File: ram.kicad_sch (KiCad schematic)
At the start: 1 part, among them U20 74LS157

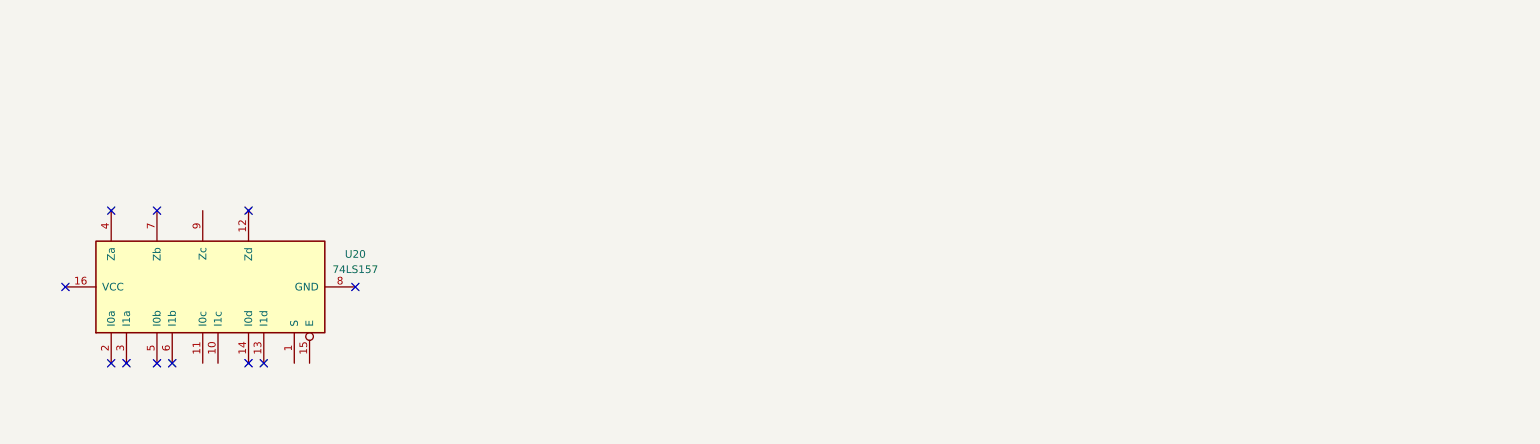
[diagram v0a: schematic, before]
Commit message: Made the ram module as well as set up a custom symbol for the 74f189sj chip.
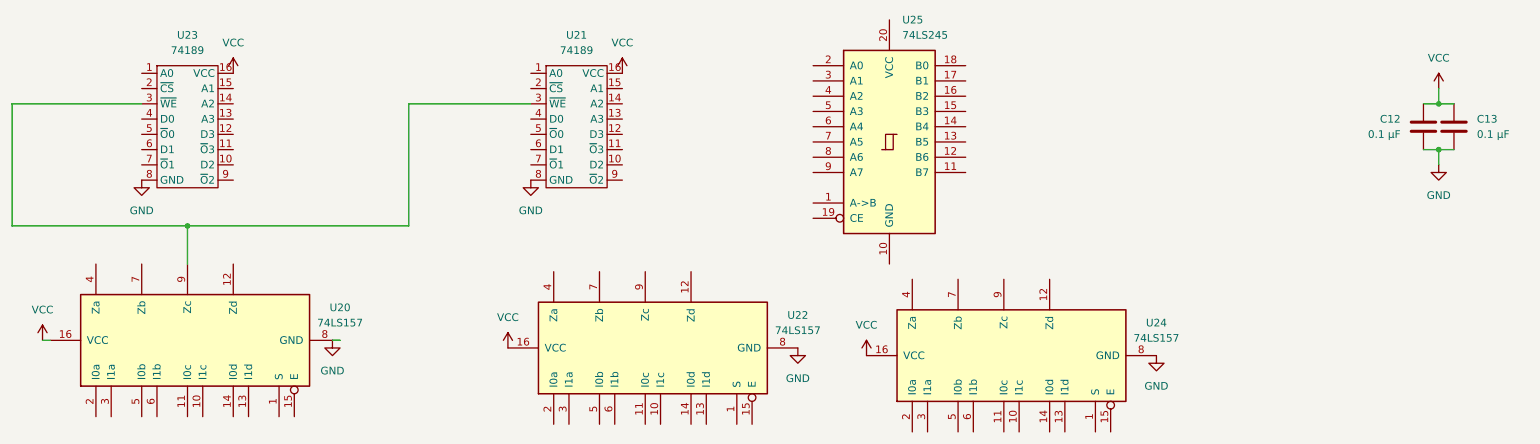
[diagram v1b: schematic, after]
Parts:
- added C12, C13: 0.1 µF, symbol Device:C
- added U21, U23: 74189, symbol Custom:74F189SJ
- added U22, U24: 74LS157, symbol 74xx:74LS157
- added U25: 74LS245, symbol 74xx:74LS245
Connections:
- net VCC: now reaches U20.16 (VCC)
- net VCC: now also C12.1, C13.1, U21.16 (VCC), U22.16 (VCC), U23.16 (VCC), U24.16 (VCC)
- net GND: now reaches U20.8 (GND)
- net GND: now also C12.2, C13.2, U21.8 (GND), U22.8 (GND), U23.8 (GND), U24.8 (GND)
- net at U20.9 (Zc): now also U21.3 (~{WE}), U23.3 (~{WE})
- no-connect marks 11 -> 0

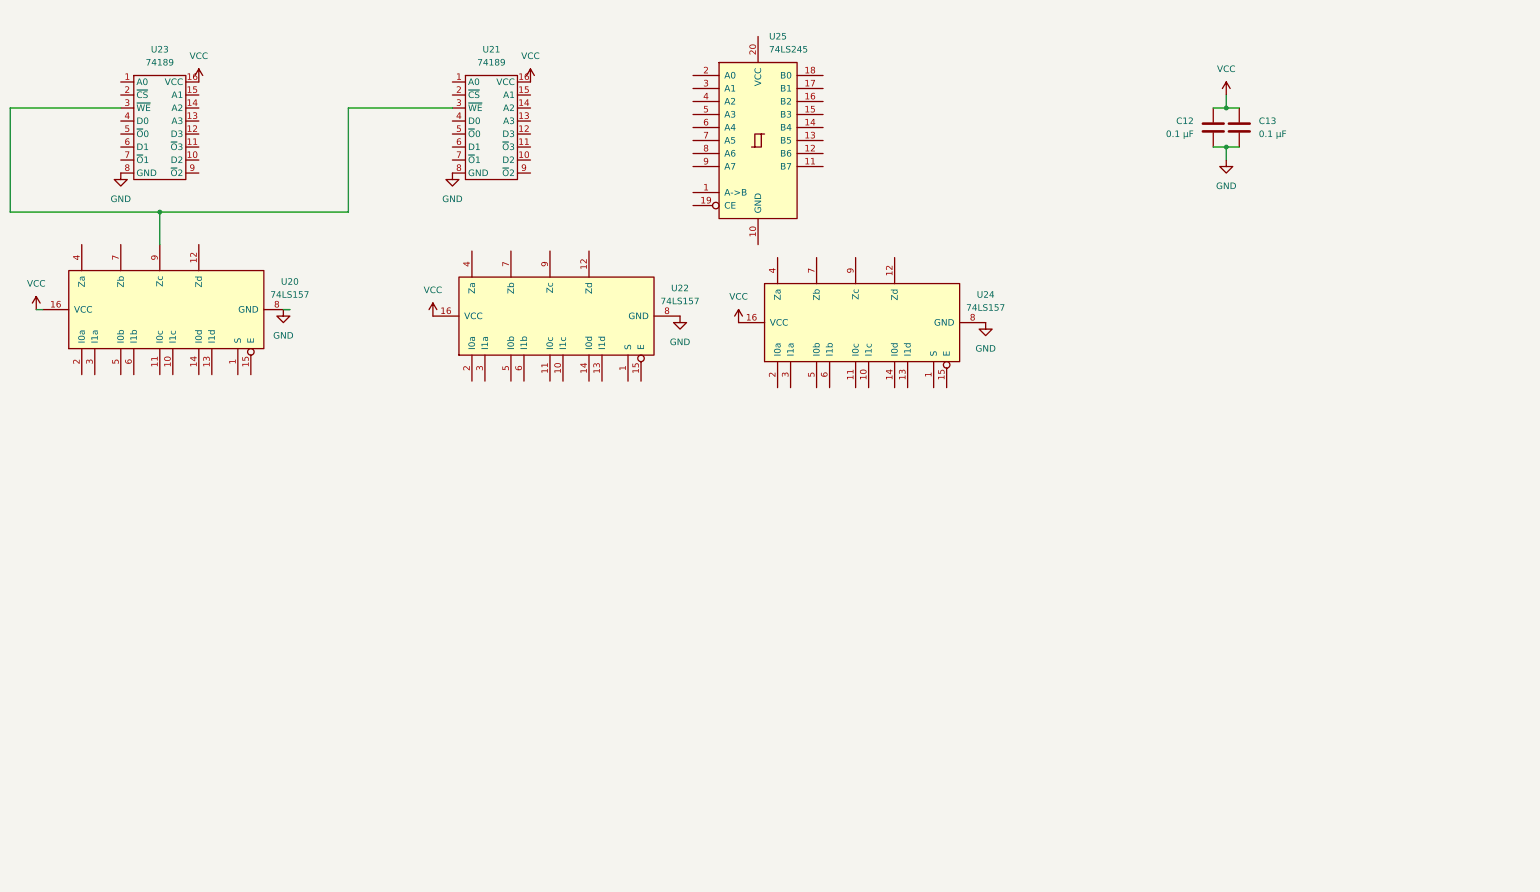
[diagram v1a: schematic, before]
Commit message: Added the program counter
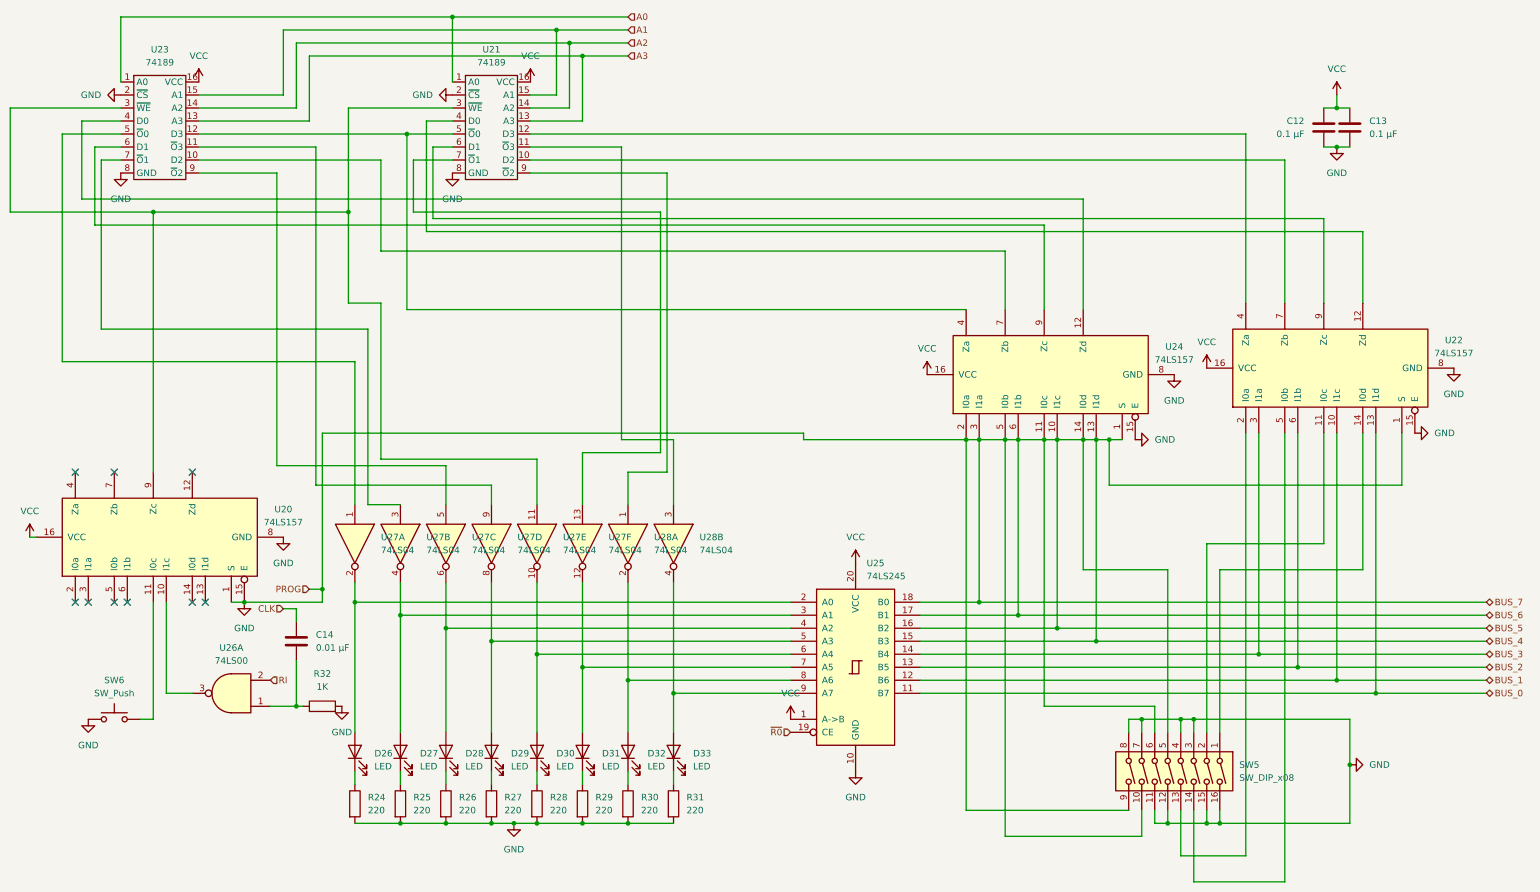
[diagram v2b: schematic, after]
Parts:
- added C14: 0.01 µF, symbol Device:C
- added D26, D27, D28, D29, D30, D31, D32, D33: LED, symbol Device:LED
- added R24, R25, R26, R27, R28, R29, R30, R31: 220, symbol Device:R
- added R32: 1K, symbol Device:R
- added SW5: SW_DIP_x08, symbol Switch:SW_DIP_x08
- added SW6: SW_Push, symbol Switch:SW_Push
- added U26: 74LS00, symbol 74xx:74LS00
- added U27, U28: 74LS04, symbol 74xx:74LS04
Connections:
- net GND: now also U20.1 (S), U20.15 (E), U21.2 (~{CS}), U22.1 (S), U22.15 (E), U23.2 (~{CS}), U24.1 (S), U24.10 (I1c), U24.11 (I0c), U24.13 (I1d), U24.14 (I0d), U24.15 (E), U24.2 (I0a), U24.3 (I1a), U24.5 (I0b), U24.6 (I1b), U25.10 (GND), U25.15 (B3), U25.16 (B2), U25.17 (B1), U25.18 (B0), R24.2, R25.2, R26.2, R27.2, R28.2, R29.2, R30.2, R31.2, R32.2, SW5.10, SW5.11, SW5.12, SW5.15, SW5.16, SW5.3, SW5.4, SW5.5, SW5.6, SW5.7, SW5.8, SW5.9, SW6.1
- net VCC: now also U25.1 (A->B), U25.20 (VCC)
- net A0: now reaches U21.1 (A0)
- net A0: now also U23.1 (A0)
- net at U21.10 (D2): now also U22.7 (Zb)
- net at U21.11 (~{O}3): now also U28.3
- net at U21.12 (D3): now also U22.4 (Za)
- net A3: now reaches U21.13 (A3)
- net A3: now also U23.13 (A3)
- net A2: now reaches U21.14 (A2)
- net A2: now also U23.14 (A2)
- net A1: now reaches U21.15 (A1)
- net A1: now also U23.15 (A1)
- net at U20.9 (Zc), U21.3 (~{WE}), U23.3 (~{WE}): now also U27.11
- net at U21.4 (D0): now also U22.12 (Zd)
- net at U21.5 (~{O}0): now also U23.12 (D3), U24.4 (Za)
- net at U21.6 (D1): now also U22.9 (Zc)
- net at U21.7 (~{O}1): now also U27.13
- net at U21.9 (~{O}2): now also U28.1
- net at U23.10 (D2): now also U24.7 (Zb)
- net at U23.11 (~{O}3): now also U27.9
- net at U23.4 (D0): now also U24.12 (Zd)
- net at U23.5 (~{O}0): now also U27.1
- net at U23.6 (D1): now also U24.9 (Zc)
- net at U23.7 (~{O}1): now also U27.3
- net at U23.9 (~{O}2): now also U27.5
- net BUS_1: now reaches U22.10 (I1c)
- net BUS_1: now also U25.12 (B6)
- net at U22.11 (I0c): now also SW5.2
- net BUS_0: now reaches U22.13 (I1d)
- net BUS_0: now also U25.11 (B7)
- net at U22.14 (I0d): now also SW5.1
- net at U22.2 (I0a): now also SW5.13
- net BUS_3: now reaches U22.3 (I1a)
- net BUS_3: now also U25.14 (B4)
- net at U22.5 (I0b): now also SW5.14
- net BUS_2: now reaches U22.6 (I1b)
- net BUS_2: now also U25.13 (B5)
- net ~{R0}: now reaches U25.19 (CE)
- net at U25.2 (A0): now also D26.2 (A), U27.2
- net at U25.3 (A1): now also D27.2 (A), U27.4
- net at U25.4 (A2): now also D28.2 (A), U27.6
- net at U25.5 (A3): now also D29.2 (A), U27.8
- net at U25.6 (A4): now also D30.2 (A), U27.10
- net at U25.7 (A5): now also D31.2 (A), U27.12
- net at U25.8 (A6): now also D32.2 (A), U28.2
- net at U25.9 (A7): now also D33.2 (A), U28.4
- net at U20.10 (I1c): now also U26.3
- net at U20.11 (I0c): now also SW6.2
- new net: C14.2, R32.1, U26.1
- new net: D27.1 (K), R25.1
- new net: D33.1 (K), R31.1
- new net: D32.1 (K), R30.1
- new net: D26.1 (K), R24.1
- new net: D30.1 (K), R28.1
- new net: D31.1 (K), R29.1
- new net: D28.1 (K), R26.1
- new net: D29.1 (K), R27.1
- new net CLK: C14.1
- new net RI: U26.2
- no-connect marks 0 -> 9
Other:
- moved on the sheet: C12, C13, U20, U22, U24, U25
